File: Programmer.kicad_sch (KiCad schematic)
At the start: 54 parts, among them J1 ZIF-socket, J2 ISP, J7 ZIF_VCC, P1 USB-C, Q2 BC327, Q4 BC327, Q5 BC327, Q6 BC327, SW1 Reset, U1 ATmega1284-P, U2 MCP2221AxP, U5 ULN2003, Y1 20M

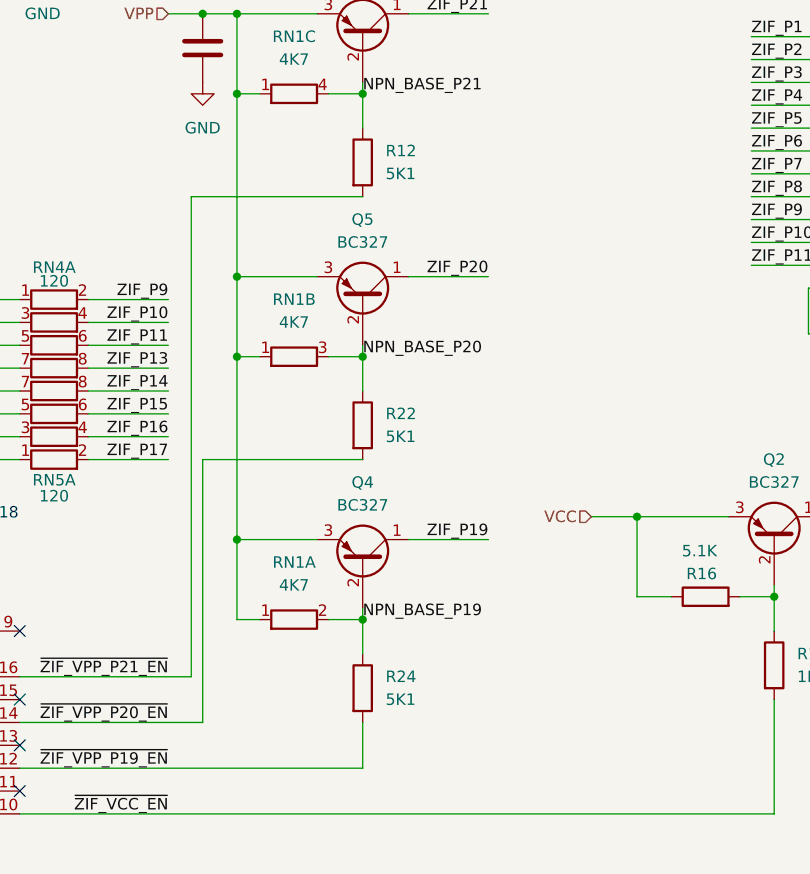
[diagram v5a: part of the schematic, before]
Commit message: Change base resistors for VPP transistors
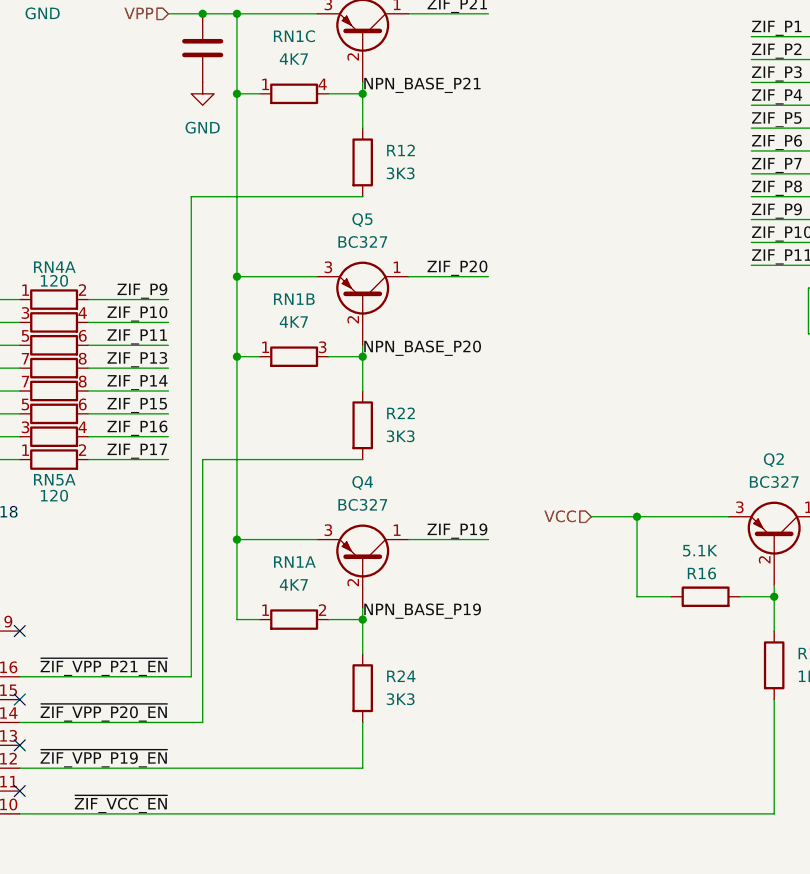
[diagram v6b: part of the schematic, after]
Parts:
- R12, R22, R24: value 5K1 -> 3K3
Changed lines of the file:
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@@
 			)
 		)
-		(property "Value" "5K1"
+		(property "Value" "3K3"
 			(at 173.99 93.98 0)
 			(effects
@@
 			)
 		)
-		(property "Value" "5K1"
+		(property "Value" "3K3"
 			(at 173.99 123.19 0)
 			(effects
@@
 			)
 		)
-		(property "Value" "5K1"
+		(property "Value" "3K3"
 			(at 173.99 152.4 0)
 			(effects

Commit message: Start working on hw revision 1.4
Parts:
- removed D11, D12, D13, D14, D15, D16, D17, D18: 4v7, Diode_THT:D_DO-35_SOD27_P7.62mm_Horizontal, symbol Device:D_Zener_Small
- removed RN2, RN3: 120, Resistor_THT:R_Array_SIP8, symbol Device:R_Pack04_SIP_Split
- added D11, D12, D13, D14, D15, D16, D17, D18: SD103A, Diode_THT:D_DO-35_SOD27_P7.62mm_Horizontal, symbol Device:D_Schottky_Small
- RN4, RN5: value 120 -> 220
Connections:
- net +5V: now also D11.1 (K), D12.1 (K), D13.1 (K), D14.1 (K), D15.1 (K), D16.1 (K), D17.1 (K), D18.1 (K)
- net MCU_P10: now also RN4.3 (R2.1), D17.2 (A)
- net MCU_P11: now also RN4.5 (R3.1), D16.2 (A)
- net MCU_P13: now also RN4.7 (R4.1), D15.2 (A)
- net MCU_P14: now also RN5.7 (R4.1), D14.2 (A)
- net MCU_P15: now also RN5.5 (R3.1), D13.2 (A)
- net MCU_P16: now also RN5.3 (R2.1), D12.2 (A)
- net MCU_P17: now also RN5.1 (R1.1), D11.2 (A)
- net MCU_P9: now also RN4.1 (R1.1), D18.2 (A)
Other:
- note added: "D11-D18 SD103A"
- note removed: "8x D11-D18 4v7"
- moved on the sheet: D4, D6

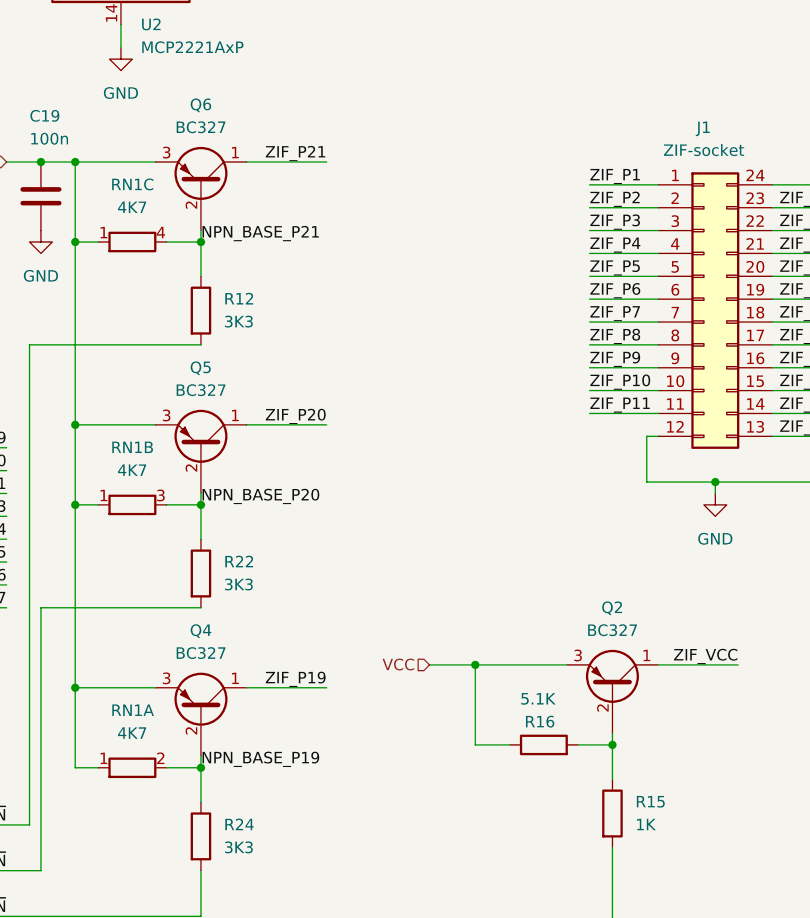
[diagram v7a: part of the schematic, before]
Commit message: Fixes after KiCad 9 upgrade
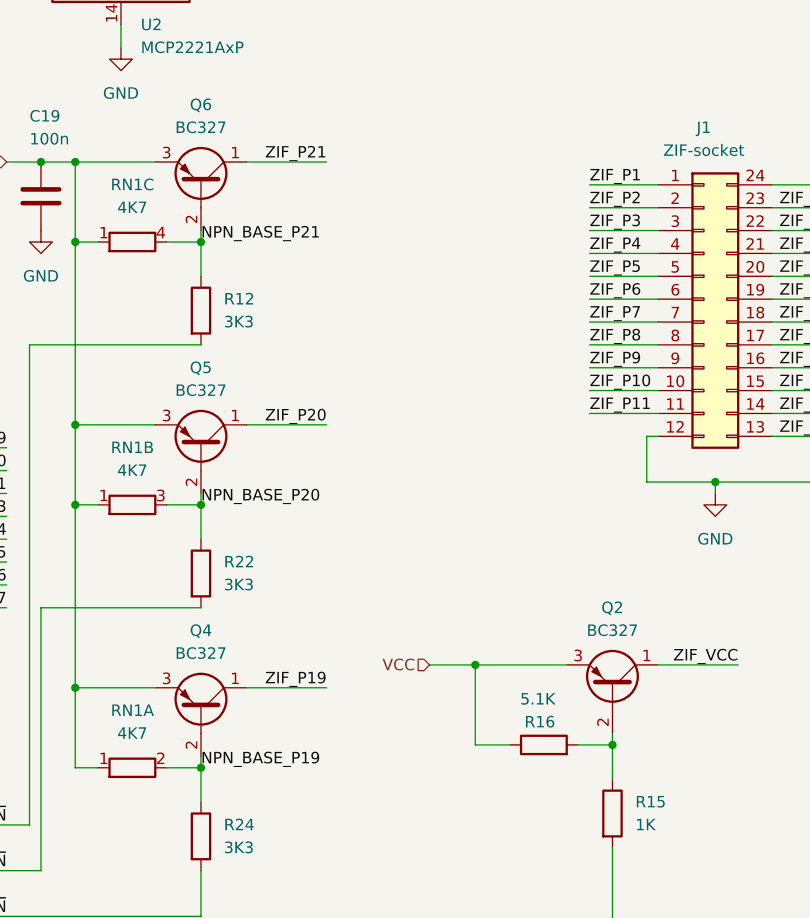
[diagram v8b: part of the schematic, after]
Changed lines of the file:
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@@
 	)
 	(symbol
-		(lib_name "GND_1")
 		(lib_id "power:GND")
 		(at 25.4 92.71 0)
@@
 			)
 		)
-		(property "Description" ""
+		(property "Description" "100V 0.15A standard switching diode, DO-35"
 			(at 86.36 148.59 0)
 			(effects
@@
 			)
 		)
-		(property "Description" ""
+		(property "Description" "Unpolarized capacitor"
 			(at 19.05 46.99 0)
 			(effects
@@
 			)
 		)
-		(property "Description" ""
+		(property "Description" "Resistor"
 			(at 171.45 92.71 0)
 			(effects
@@
 	)
 	(symbol
-		(lib_name "GND_1")
 		(lib_id "power:GND")
 		(at 162.56 63.5 0)
@@
 			)
 		)
-		(property "Description" ""
+		(property "Description" "Resistor"
 			(at 252.73 104.14 0)
 			(effects
@@
 	)
 	(symbol
-		(lib_name "+5V_1")
 		(lib_id "power:+5V")
 		(at 162.56 19.05 0)
@@
 			)
 		)
-		(property "Description" ""
+		(property "Description" "Unpolarized capacitor"
 			(at 144.78 25.4 0)
 			(effects
@@
 	)
 	(symbol
-		(lib_name "GND_1")
 		(lib_id "power:GND")
 		(at 135.89 71.12 0)
@@
 			)
 		)
-		(property "Description" ""
+		(property "Description" "Resistor"
 			(at 138.43 60.96 0)
 			(effects
@@
 			)
 		)
-		(property "Description" ""
+		(property "Description" "Push button switch, generic, two pins"
 			(at 25.4 62.23 0)
 			(effects
@@
 			)
 		)
-		(property "Description" ""
+		(property "Description" "20MHz, 128kB Flash, 16kB SRAM, 4kB EEPROM, JTAG, DIP-40"
 			(at 58.42 105.41 0)
 			(effects
@@
 			)
 		)
-		(property "Description" ""
+		(property "Description" "Generic connector, single row, 01x01, script generated"
 			(at 250.19 67.31 0)
 			(effects
@@
 	)
 	(symbol
-		(lib_name "+5V_1")
 		(lib_id "power:+5V")
 		(at 46.99 41.91 0)
@@
 	)
 	(symbol
-		(lib_name "GND_1")
 		(lib_id "power:GND")
 		(at 109.22 76.2 0)
@@
 			)
 		)
-		(property "Description" ""
+		(property "Description" "Resistor"
 			(at 217.17 148.59 0)
 			(effects
@@
 			)
 		)
-		(property "Description" ""
+		(property "Description" "Resistor"
 			(at 209.55 140.97 0)
 			(effects
@@
 			)
 		)
-		(property "Description" ""
+		(property "Description" "Light emitting diode"
+			(at 212.09 34.29 0)
+			(effects
+				(font
+					(size 1.27 1.27)
+				)
+				(hide yes)
+			)
+		)
+		(property "Sim.Pins" "1=K 2=A"
 			(at 212.09 34.29 0)
 			(effects
@@
 			)
 		)
-		(property "Description" ""
+		(property "Description" "Unpolarized capacitor"
 			(at 26.67 46.99 0)
 			(effects
@@
 			)
 		)
-		(property "Description" ""
+		(property "Description" "Resistor"
 			(at 171.45 121.92 0)
 			(effects
@@
 			)
 		)
-		(property "Description" ""
+		(property "Description" "0.8A Ic, 45V Vce, PNP Transistor, TO-92"
 			(at 171.45 78.74 0)
 			(effects
@@
 			)
 		)
-		(property "Description" ""
+		(property "Description" "0.8A Ic, 45V Vce, PNP Transistor, TO-92"
 			(at 217.17 134.62 0)
 			(effects
@@
 	)
 	(symbol
-		(lib_name "+5V_1")
 		(lib_id "power:+5V")
 		(at 39.37 109.22 0)
@@
 	)
 	(symbol
-		(lib_name "GND_1")
 		(lib_id "power:GND")
 		(at 153.67 83.82 0)
@@
 	)
 	(symbol
-		(lib_name "GND_1")
 		(lib_id "power:GND")
 		(at 58.42 160.02 0)
@@
 			)
 		)
-		(property "Description" ""
+		(property "Description" "Unpolarized capacitor"
 			(at 20.32 83.82 0)
 			(effects
@@
 	)
 	(symbol
-		(lib_name "GND_1")
 		(lib_id "power:GND")
 		(at 212.09 50.8 0)
@@
 			)
 		)
-		(property "Description" ""
+		(property "Description" "USB 2.0-only Type-C Receptacle connector"
 			(at 109.22 50.8 0)
 			(effects
@@
 			)
 		)
-		(property "Description" ""
+		(property "Description" "Resistor"
 			(at 212.09 44.45 0)
 			(effects
@@
 	)
 	(symbol
-		(lib_name "GND_1")
 		(lib_id "power:GND")
 		(at 144.78 29.21 0)
@@
 	)
 	(symbol
-		(lib_name "GND_1")
 		(lib_id "power:GND")
 		(at 22.86 50.8 0)
@@
 			)
 		)
-		(property "Description" ""
+		(property "Description" "Generic connector, double row, 02x12, counter clockwise pin numbering scheme (similar to DIP package numbering), script generated (kicad-library-utils/schlib/autogen/connector/)"
 			(at 227.33 91.44 0)
 			(effects
@@
 	)
 	(symbol
-		(lib_name "GND_1")
 		(lib_id "power:GND")
 		(at 228.6 113.03 0)
@@
 			)
 		)
-		(property "Description" ""
+		(property "Description" "Two pin crystal"
 			(at 25.4 76.2 0)
 			(effects
@@
 			)
 		)
-		(property "Description" ""
+		(property "Description" "100V 0.15A standard switching diode, DO-35"
 			(at 96.52 92.71 0)
 			(effects
@@
 			)
 		)
-		(property "Description" ""
+		(property "Description" "Unpolarized capacitor"
 			(at 153.67 80.01 0)
 			(effects
@@
 	)
 	(symbol
-		(lib_name "+5V_1")
 		(lib_id "power:+5V")
 		(at 212.09 27.94 0)
@@
 	)
 	(symbol
-		(lib_name "+5V_1")
 		(lib_id "power:+5V")
 		(at 198.12 27.94 0)
@@
 	)
 	(symbol
-		(lib_name "GND_1")
 		(lib_id "power:GND")
 		(at 123.19 172.72 0)
@@
 			)
 		)
-		(property "Description" ""
+		(property "Description" "Resistor"
 			(at 41.91 52.07 0)
 			(effects
@@
 			)
 		)
-		(property "Description" ""
+		(property "Description" "Resistor"
 			(at 194.31 44.45 0)
 			(effects
@@
 	)
 	(symbol
-		(lib_name "+5V_1")
 		(lib_id "power:+5V")
 		(at 110.49 99.06 0)
@@
 			)
 		)
-		(property "Description" ""
+		(property "Description" "Resistor"
 			(at 133.35 60.96 0)
 			(effects
@@
 			)
 		)
-		(property "Description" ""
+		(property "Description" "Resistor"
 			(at 201.93 44.45 0)
 			(effects
@@
 	)
 	(symbol
-		(lib_name "GND_1")
 		(lib_id "power:GND")
 		(at 39.37 125.73 0)
@@
 			)
 		)
-		(property "Description" ""
+		(property "Description" "0.8A Ic, 45V Vce, PNP Transistor, TO-92"
 			(at 171.45 107.95 0)
 			(effects
@@
 			)
 		)
-		(property "Description" ""
+		(property "Description" "Light emitting diode"
+			(at 194.31 34.29 0)
+			(effects
+				(font
+					(size 1.27 1.27)
+				)
+				(hide yes)
+			)
+		)
+		(property "Sim.Pins" "1=K 2=A"
 			(at 194.31 34.29 0)
 			(effects
@@
 			)
 		)
-		(property "Description" ""
+		(property "Description" "Resistor"
 			(at 247.65 104.14 0)
 			(effects
@@
 	)
 	(symbol
-		(lib_name "GND_1")
 		(lib_id "power:GND")
 		(at 179.07 33.02 0)
@@
 			)
 		)
-		(property "Description" ""
+		(property "Description" "0.8A Ic, 45V Vce, PNP Transistor, TO-92"
 			(at 171.45 137.16 0)
 			(effects
@@
 			)
 		)
-		(property "Description" ""
+		(property "Description" "Light emitting diode"
+			(at 201.93 34.29 0)
+			(effects
+				(font
+					(size 1.27 1.27)
+				)
+				(hide yes)
+			)
+		)
+		(property "Sim.Pins" "1=K 2=A"
 			(at 201.93 34.29 0)
 			(effects
@@
 			)
 		)
-		(property "Description" ""
+		(property "Description" "Resistor"
 			(at 171.45 151.13 0)
 			(effects
@@
 			)
 		)
-		(property "Description" ""
+		(property "Description" "USB to I2C/UART Protocol Converter with GPIO, DIP-14"
 			(at 162.56 45.72 0)
 			(effects
@@
 			)
 		)
-		(property "Description" ""
+		(property "Description" "100V 0.15A standard switching diode, DO-35"
 			(at 96.52 95.25 0)
 			(effects
@@
 			)
 		)
-		(property "Description" ""
+		(property "Description" "Unpolarized capacitor"
 			(at 179.07 29.21 0)
 			(effects
@@
 			)
 		)
-		(property "Description" ""
+		(property "Description" "Generic connector, double row, 02x03, odd/even pin numbering scheme (row 1 odd numbers, row 2 even numbers), script generated (kicad-library-utils/schlib/autogen/connector/)"
 			(at 29.21 118.11 0)
 			(effects
@@
 			)
 		)
-		(property "Description" ""
+		(property "Description" "Unpolarized capacitor"
 			(at 30.48 83.82 0)
 			(effects
@@
 			)
 		)
-		(property "Description" ""
+		(property "Description" "Resistor"
 			(at 257.81 104.14 0)
 			(effects
@@
 			)
 		)
-		(property "Description" ""
+		(property "Description" "Unpolarized capacitor"
 			(at 250.19 76.2 0)
 			(effects
@@
 	)
 	(symbol
-		(lib_name "GND_1")
 		(lib_id "power:GND")
 		(at 250.19 80.01 0)
